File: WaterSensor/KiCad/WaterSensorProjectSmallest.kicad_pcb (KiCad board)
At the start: 2 copper layers, 51 x 14 mm, 17 parts, among them Q1_A1 TEPT4400, Q1_B1 TEPT4400, U1 RP604K331A-TR, U2 ESP32-C3-MINI-1-N4, U3 TLV7042DDFR

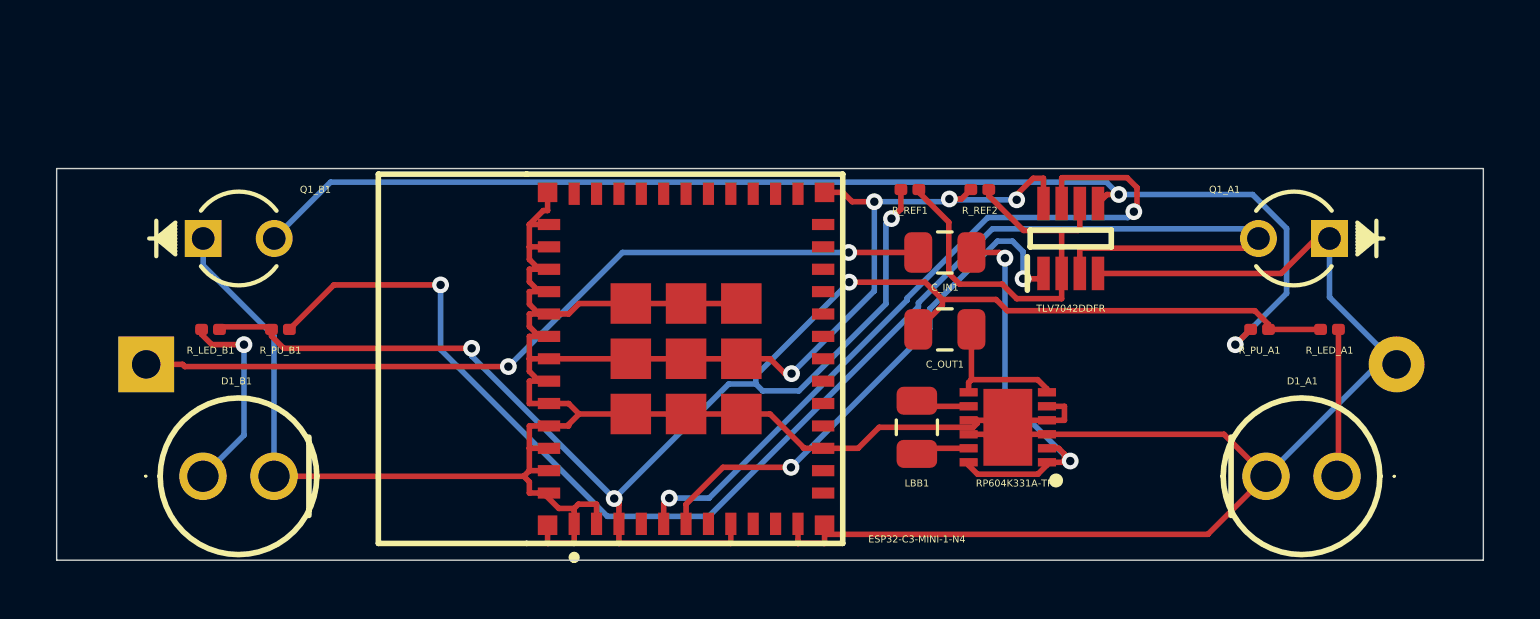
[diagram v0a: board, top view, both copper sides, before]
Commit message: Alternate designs and pcbs based on different battery sizes
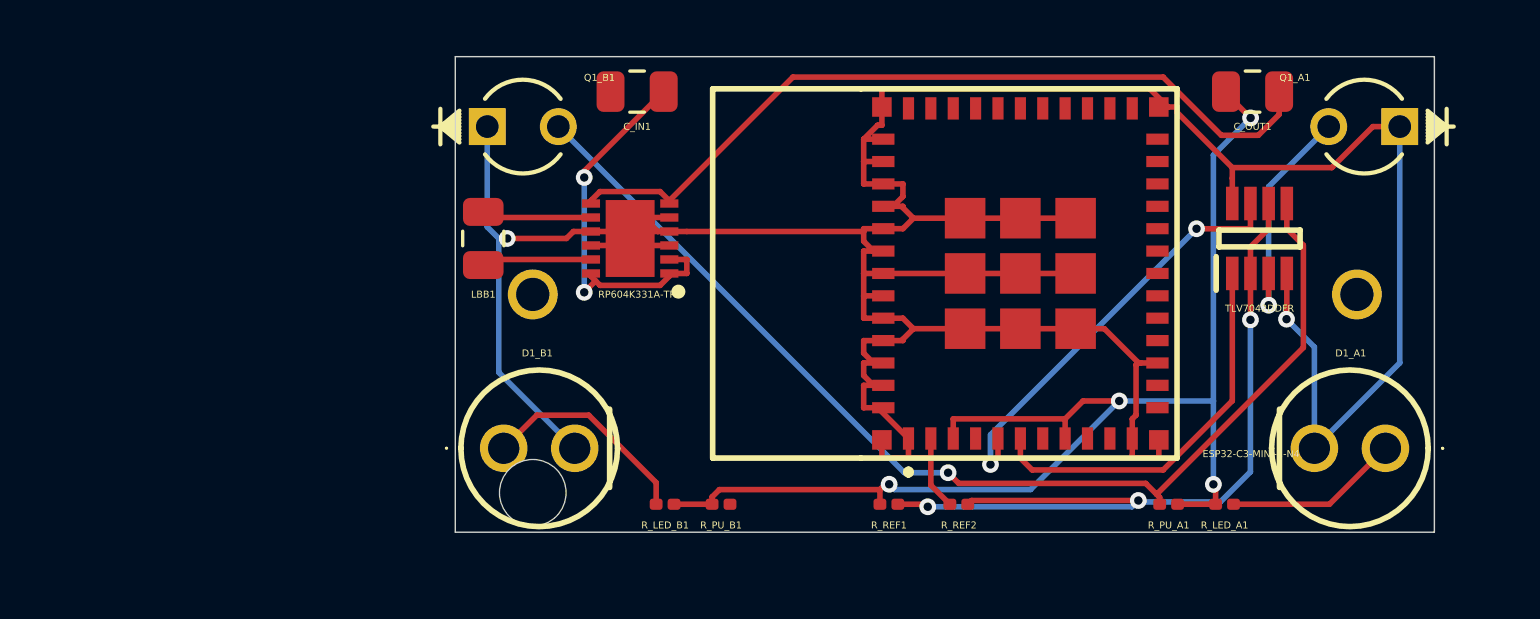
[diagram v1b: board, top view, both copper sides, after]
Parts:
- Battery1: footprint Battery:BatteryHolder_Keystone_2466_1xAAA -> 108:BAT_108
- moved Battery1 28.7 mm to (107.2, 91.5)
- moved R_LED_B1 17.4 mm to (97.2, 99.0)
- moved R_PU_B1 16.9 mm to (99.2, 99.0)
- moved LBB1 16.9 mm to (90.8, 89.5)
- moved U1 15.1 mm to (96.0, 89.5)
- moved C_OUT1 13.9 mm to (118.2, 84.2)
- moved C_IN1 12.4 mm to (96.2, 84.2)
- moved U2 12.3 mm to (110.0, 90.8)
- moved R_REF1 11.3 mm to (105.2, 99.0)
- moved R_REF2 11.3 mm to (107.8, 99.0)
- moved Q1_B1 10.9 mm to (90.9, 85.5)
- moved D1_B1 10.8 mm to (92.8, 97.0)
- moved R_LED_A1 7.29 mm to (117.2, 99.0)
- moved R_PU_A1 7.04 mm to (115.2, 99.0)
- moved U3 6.75 mm to (118.5, 89.5)
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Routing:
- net Net-(U3-INA+): track 52.0 -> 8.41 mm
- net Net-(Battery1-+): track 29.3 -> 0.00 mm, vias 2 -> 0
- net Net-(U1-VFB): track 5.25 -> 28.9 mm
- net Net-(Battery1--): track 150.9 -> 130.7 mm, vias 4 -> 2
- net Net-(U2-3V3): track 64.6 -> 46.3 mm
- net Net-(U3-INA-): track 15.2 -> 29.2 mm, vias 0 -> 3
- net Net-(U2-IO2): track 26.6 -> 15.4 mm
- net Net-(U2-IO3): track 19.0 -> 14.0 mm, vias 2 -> 0
- net Net-(U3-INB+): track 44.3 -> 40.0 mm, vias 2 -> 1
- net Net-(U1-BULX): track 1.93 -> 3.93 mm
- net Net-(U1-BOLX): track 1.93 -> 3.93 mm
- net Net-(D1_A1-A): track 5.27 -> 6.26 mm
- net Net-(U1-AVIN): track 14.6 -> 14.0 mm
- net Net-(D1_B1-A): track 7.16 -> 7.71 mm, vias 1 -> 0
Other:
- board size 51 x 14 mm -> 35 x 17 mm
